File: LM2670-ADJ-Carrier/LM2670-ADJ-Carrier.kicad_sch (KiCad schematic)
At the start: 11 parts, among them IC1 LM2670SX-3.3_NOPB, J1 Conn_01x03

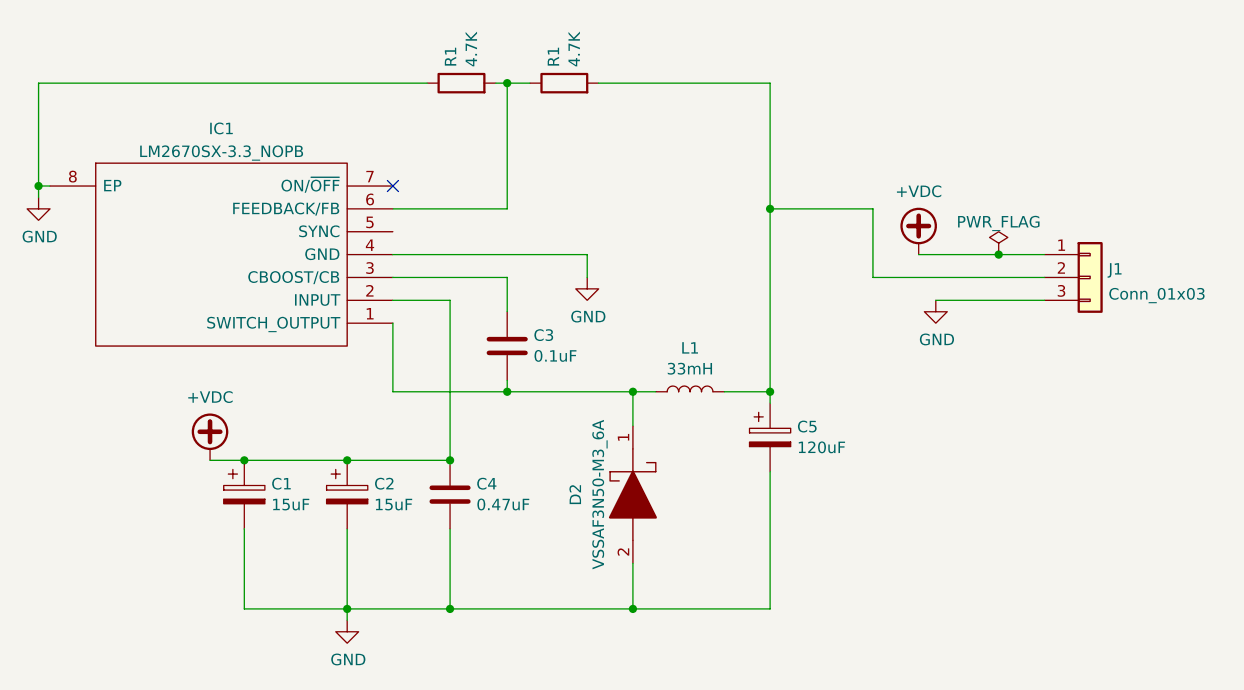
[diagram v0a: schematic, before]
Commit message: finished ADJ board and adding the Fab Files for it.
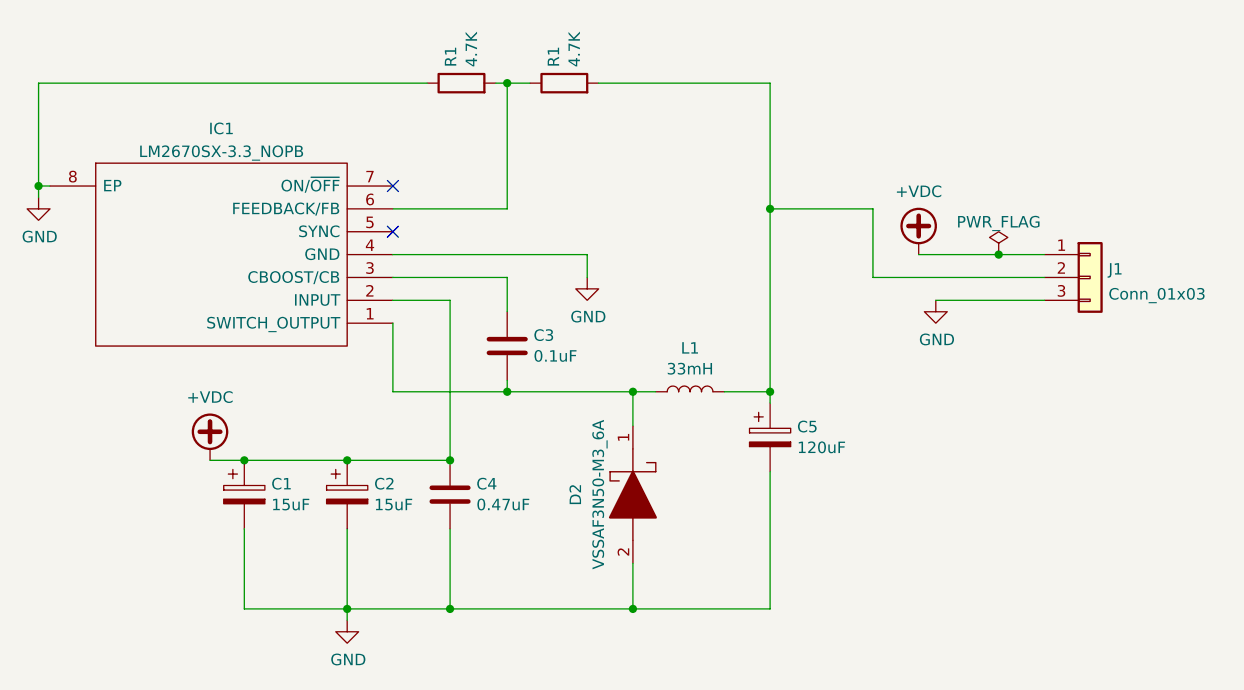
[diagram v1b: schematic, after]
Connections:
- no-connect marks 1 -> 2
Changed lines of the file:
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@@
   )
   (no_connect (at 121.92 81.28))
+  (no_connect (at 121.92 86.36))
   (wire (pts (xy 175.26 91.44) (xy 175.26 83.82))
     (stroke (width 0) (type default))

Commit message: update footprints in schematic only
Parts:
- C3, C4: footprint Capacitor_SMD:C_0603_1608Metric_Pad1.08x0.95mm_HandSolder -> Capacitor_SMD:C_1206_3216Metric_Pad1.33x1.80mm_HandSolder
- R1: footprint Resistor_SMD:R_0612_1632Metric_Pad1.18x3.40mm_HandSolder -> Resistor_SMD:R_1206_3216Metric_Pad1.30x1.75mm_HandSolder
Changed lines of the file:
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@@
 			)
 		)
-		(property "Footprint" "Resistor_SMD:R_0612_1632Metric_Pad1.18x3.40mm_HandSolder"
+		(property "Footprint" "Resistor_SMD:R_1206_3216Metric_Pad1.30x1.75mm_HandSolder"
 			(at 140.97 71.628 90)
 			(effects
@@
 			)
 		)
-		(property "Footprint" "Capacitor_SMD:C_0603_1608Metric_Pad1.08x0.95mm_HandSolder"
+		(property "Footprint" "Capacitor_SMD:C_1206_3216Metric_Pad1.33x1.80mm_HandSolder"
 			(at 129.2352 119.38 0)
 			(effects
@@
 			)
 		)
-		(property "Footprint" "Capacitor_SMD:C_0603_1608Metric_Pad1.08x0.95mm_HandSolder"
+		(property "Footprint" "Capacitor_SMD:C_1206_3216Metric_Pad1.33x1.80mm_HandSolder"
 			(at 135.5852 102.87 0)
 			(effects
@@
 			)
 		)
-		(property "Footprint" "Resistor_SMD:R_0612_1632Metric_Pad1.18x3.40mm_HandSolder"
+		(property "Footprint" "Resistor_SMD:R_1206_3216Metric_Pad1.30x1.75mm_HandSolder"
 			(at 129.54 71.628 90)
 			(effects
